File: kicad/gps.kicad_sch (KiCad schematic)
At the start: 68 parts, among them J1 Bus_PCI_Express_x1, J2 USB_C_Receptacle_USB2.0_16P, J3 Conn_01x02, J4 USB_C_Receptacle_USB2.0_16P, Q1 IRLML6344, U2 W25Q128JVP, U3 MCP25625T-E/ML, U4 RP2040, U5 NEO-M9N, X1 ABM8-272-T3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

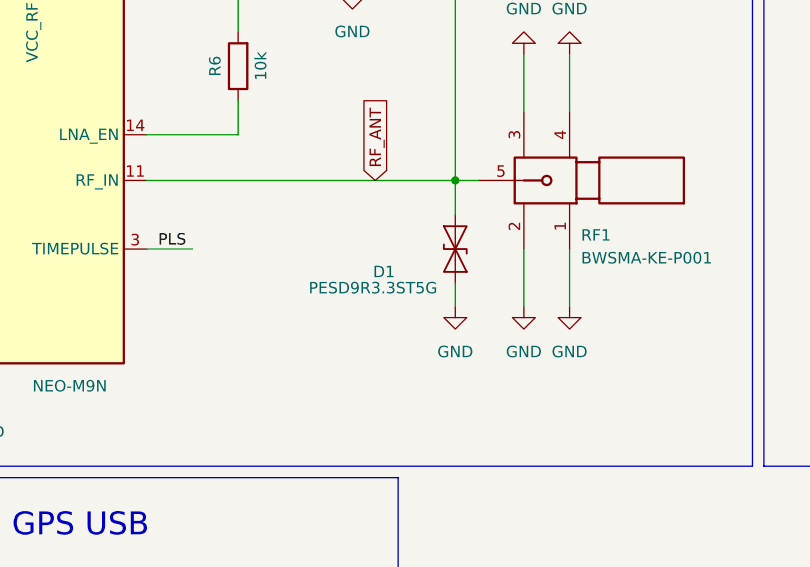
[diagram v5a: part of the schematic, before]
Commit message: Add TVS Diode to footprint
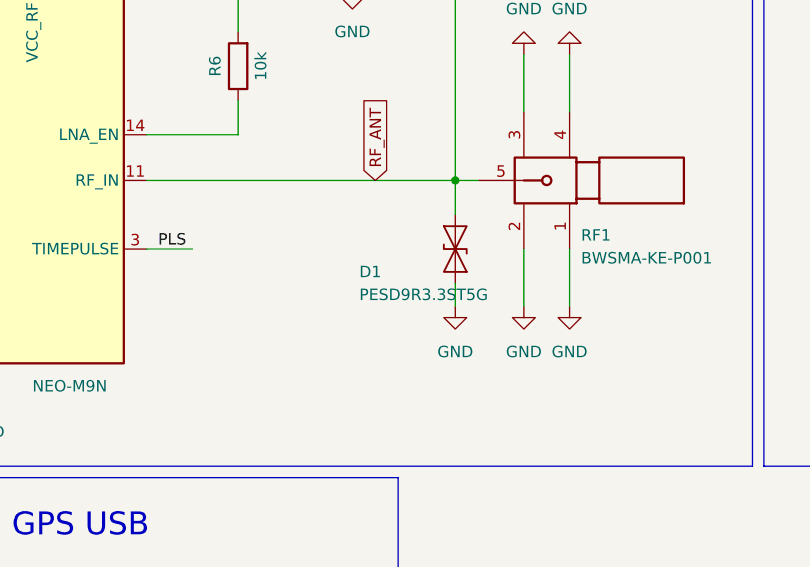
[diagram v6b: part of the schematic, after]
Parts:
- D1: footprint Package_TO_SOT_SMD:SOD-923 -> Diode_SMD:D_SOD-923; Current Draw 0 (leakage only) -> (none)
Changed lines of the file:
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@@
 		(dnp no)
 		(property "Reference" "D1"
-			(at 295.656 78.74 90)
+			(at 294.132 78.74 90)
 			(effects
 				(font
@@
 		)
 		(property "Value" "PESD9R3.3ST5G"
-			(at 295.656 81.28 90)
+			(at 294.132 81.28 90)
 			(effects
 				(font
 					(size 1.27 1.27)
 				)
-				(justify top)
+				(justify right)
 			)
 		)
-		(property "Footprint" "Package_TO_SOT_SMD:SOD-923"
+		(property "Footprint" "Diode_SMD:D_SOD-923"
 			(at 304.8 76.2 0)
 			(effects
@@
 					(size 1.27 1.27)
 				)
-				(justify bottom)
 				(hide yes)
 			)
@@
 			(at 304.8 76.2 90)
 			(effects
-				(font
-					(size 1.27 1.27)
-				)
-				(justify top)
-				(hide yes)
-			)
-		)
-		(property "Current Draw" "0 (leakage only)"
-			(at 304.8 76.2 90)
-			(effects

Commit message: Update gate resistor value and apply general BOM improvements
- Changed gate resistor R6 from 10kΩ to 2.2kΩ to improve MOSFET switching speed while maintaining safe drive current for LNA_EN pin.
- Updated associated resistor part to a 0402 UNI-ROYAL 2.2kΩ variant with high stock from JLCPCB.
- Refined BOM fields for several components including RF connector (RF1) and battery holder (BAT1) to match R5 formatting.
- Ensured consistent metadata across all key parts: datasheets, LCSC part numbers, and manufacturer info.
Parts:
- BAT1: ADD INTO BOM yes -> (none); Basic? (none) -> No; CONVERT TO PCB yes -> (none); Current Draw (none) -> N/A (mechanical component); DEVICE 2998 -> (none); Height (none) -> Not listed; JLC Link (none) -> https://jlcpcb.com/partdetail/C238096; JLCPCB PART CLASS Extended Part -> (none); LCSC PART NAME 2998 -> (none); LCSC Part # (none) -> C238096; MANUFACTURER Keystone -> (none); MANUFACTURER PART 2998 -> (none); Manufacturer Name (none) -> Keystone; Manufacturer Part Number (none) -> 2998; Mouser Part Number (none) -> Not listed; Mouser Price/Stock (none) -> Not listed; Notes (none) -> Surface-mount battery holder for backup power; RoHS complia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; Price (none) -> Not listed; SUPPLIER LCSC -> (none); SUPPLIER FOOTPRINT SMD -> (none); SUPPLIER PART C238096 -> (none); SYMBOL 2998 -> (none)
- R6: value 10k -> 2.2k; Info Thick Film Chip Resistor, 10 kΩ, 0402 package, ±1% toleranc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 -> 62.5mW Thick Film Resistors 50V ±100ppm/℃ ±1% 2.2kΩ 0402 Ch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; JLC Link https://jlcpcb.com/partdetail/C25744 -> https://jlcpcb.com/partdetail/C25879; LCSC Part # C25744 -> C25879; Manufacturer Part Number 0402WGF1002TCE -> 0402WGF2201TCE
- RF1: ADD INTO BOM yes -> (none); Basic? (none) -> No; CONNECTOR TYPE Board-End -> (none); CONVERT TO PCB yes -> (none); Current Draw (none) -> N/A (passive component); DEVICE BWSMA-KE-P001 -> (none); FREQUENCY-MAX - -> (none); Height (none) -> Not specified; IMPEDANCE 50Ω -> (none); INTERFACE DIAMETER 5.2mm -> (none); INTERFACE LENGTH/HEIGHT - -> (none); INTERFACE TYPE Inner Hole -> (none); JLC Link (none) -> https://jlcpcb.com/partdetail/C496550; JLCPCB PART CLASS Extended Part -> (none); LCSC PART NAME 内孔 SMA 偏脚 -> (none); LCSC Part # (none) -> C496550; MANUFACTURER BAT WIRELESS(蝙蝠无线) -> (none); MANUFACTURER PART BWSMA-KE-P001 -> (none); Manufacturer Name (none) -> BAT WIRELESS (蝙蝠无线); Manufacturer Part Number (none) -> BWSMA-KE-P001; Mouser Part Number (none) -> Not listed; Mouser Price/Stock (none) -> Not listed; NUMBER OF PORTS 1 -> (none); Notes (none) -> Suitable for GNSS/High-Frequency RF applications; 50Ω imped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; OPERATING TEMPERATURE RANGE - -> (none); Price (none) -> Not listed; RF SERIES SMA -> (none); STYLE Staggered pins -> (none); SUPPLIER LCSC -> (none); SUPPLIER FOOTPRINT SMD -> (none); SUPPLIER PART C496550 -> (none); SYMBOL BWSMA-KE-P001 -> (none)

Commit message: Update LED Positions
Move LEDs to the front of the board for 3.3V and 5V power
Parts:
- added TP4: TP_RF, TestPoint:TestPoint_Pad_D1.0mm, symbol Connector:TestPoint
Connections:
- net RF_ANT: now also TP4.1
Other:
- note added: "GPS module 0.2.0"
- note removed: "GPS module 0.1.0"
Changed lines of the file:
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@@
 	)
 	(junction
+		(at 285.75 68.58)
+		(diameter 0)
+		(color 0 0 0 0)
+	)
+	(junction
 		(at 77.47 39.37)
 		(diameter 0)
@@
 	(wire
 		(pts
-			(xy 270.51 68.58) (xy 304.8 68.58)
+			(xy 270.51 68.58) (xy 285.75 68.58)
 		)
 		(stroke
@@
 		)
 	)
+	(wire
+		(pts
+			(xy 285.75 68.58) (xy 304.8 68.58)
+		)
+		(stroke
+			(width 0)
+			(type default)
+		)
+	)
 	(polyline
 		(pts
@@
 		)
 	)
-	(text "GPS module 0.1.0"
+	(text "GPS module 0.2.0"
 		(exclude_from_sim no)
 		(at 330.962 264.668 0)
@@
 					(unit 1)
 				)
+			)
+		)
+	)
+	(symbol
+		(lib_id "Connector:TestPoint")
+		(at 285.75 68.58 180)
+		(unit 1)
+		(exclude_from_sim no)
+		(in_bom yes)
+		(on_board yes)
+		(dnp no)
+		(property "Reference" "TP4"
+			(at 284.988 73.914 0)
+			(effects
+				(font
+					(size 1.27 1.27)
+				)
+			)
+		)
+		(property "Value" "TP_RF"
+			(at 284.988 76.2 0)
+			(effects
+				(font
+					(size 1.27 1.27)
+				)
+			)
+		)
+		(property "Footprint" "TestPoint:TestPoint_Pad_D1.0mm"
+			(at 280.67 68.58 0)
+			(effects
+				(font
+					(size 1.27 1.27)
+				)
+				(hide yes)
+			)
+		)
+		(property "Datasheet" "~"
+			(at 280.67 68.58 0)
+			(effects
+				(font
+					(size 1.27 1.27)
+				)
+				(hide yes)
+			)
+		)
+		(property "Description" ""
+			(at 285.75 68.58 0)
+			(effects
+				(font
+					(size 1.27 1.27)
+				)
+				(hide yes)
+			)
+		)
+		(pin "1"
+		)
+		(instances
+			(project "gps"
+				(path "/e1ff46b9-0cf9-4507-8034-1e95fc3013fc"
+					(reference "TP4")
+					(unit 1)
+				)
